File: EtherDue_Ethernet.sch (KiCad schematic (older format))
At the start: 32 parts, among them IC601 W5100, Q601 2N7002, U603 APX811-44UG-7, U604 HY931147C, X601 TXC 7A 25MHz 18pF

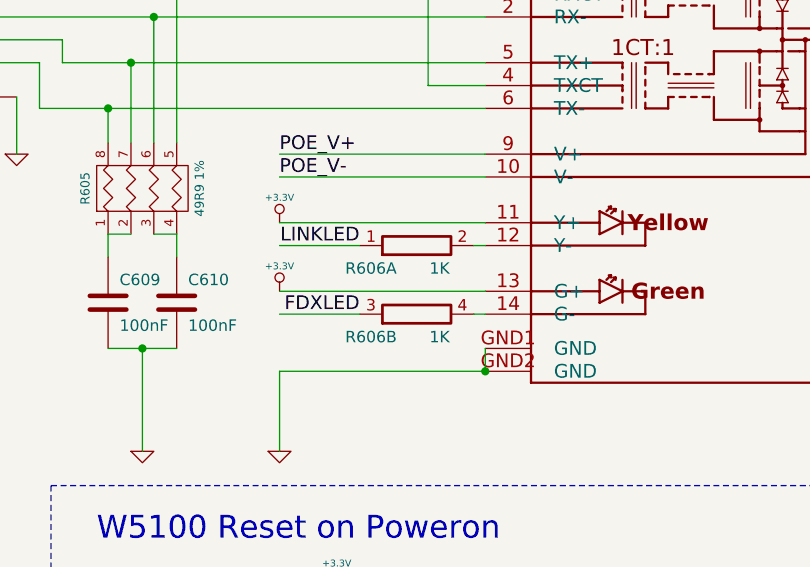
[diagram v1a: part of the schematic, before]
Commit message: Pre-autorouter hand routed traces
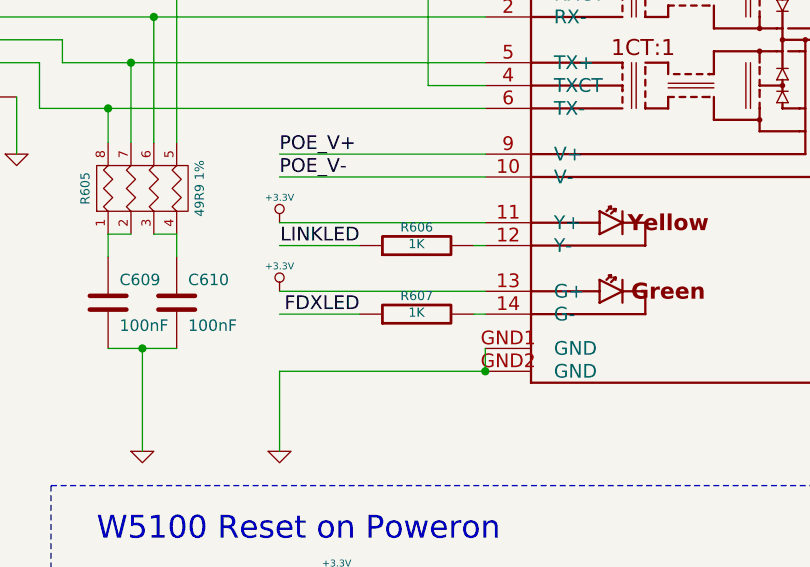
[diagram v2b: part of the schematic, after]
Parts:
- removed R606: 1K, symbol RES_PACK4_IND
- added R606, R607: 1K, ~, symbol R
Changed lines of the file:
@@
-EESchema Schematic File Version 2  date Thu 06 Jun 2013 17:31:40 EST
+EESchema Schematic File Version 2  date Wed 19 Jun 2013 10:44:48 EST
 LIBS:freetronics_kicad_sch_lib
 LIBS:power
@@
 Sheet 6 6
 Title ""
-Date "6 jun 2013"
+Date "19 jun 2013"
 Rev ""
 Comp ""
@@
 LINKLED
 $Comp
-L RES_PACK4_IND R606
-U 1 1 51663326
-P 8200 4300
-F 0 "R606" H 8000 4200 50  0000 C CNN
-F 1 "1K" H 8300 4200 50  0000 C CNN
-F 2 "" H 8200 4300 60  0001 C CNN
-F 3 "" H 8200 4300 60  0001 C CNN
-	1    8200 4300
-	1    0    0    -1
-$EndComp
-$Comp
-L RES_PACK4_IND R606
-U 2 1 51663316
-P 8200 4600
-F 0 "R606" H 8000 4500 50  0000 C CNN
-F 1 "1K" H 8300 4500 50  0000 C CNN
-F 2 "" H 8200 4600 60  0001 C CNN
-F 3 "" H 8200 4600 60  0001 C CNN
-	2    8200 4600
-	1    0    0    -1
-$EndComp
-$Comp
 L +3.3V #PWR091
 U 1 1 51663302
@@
 	1    0    0    -1
 $EndComp
+$Comp
+L R R606
+U 1 1 51C10B1D
+P 8200 4300
+F 0 "R606" V 8280 4300 40  0000 C CNN
+F 1 "1K" V 8207 4301 40  0000 C CNN
+F 2 "~" V 8130 4300 30  0000 C CNN
+F 3 "~" H 8200 4300 30  0000 C CNN
+	1    8200 4300
+	0    -1   -1   0
+$EndComp
+$Comp
+L R R607
+U 1 1 51C10B2F
+P 8200 4600
+F 0 "R607" V 8280 4600 40  0000 C CNN
+F 1 "1K" V 8207 4601 40  0000 C CNN
+F 2 "~" V 8130 4600 30  0000 C CNN
+F 3 "~" H 8200 4600 30  0000 C CNN
+	1    8200 4600
+	0    -1   -1   0
+$EndComp
 $EndSCHEMATC

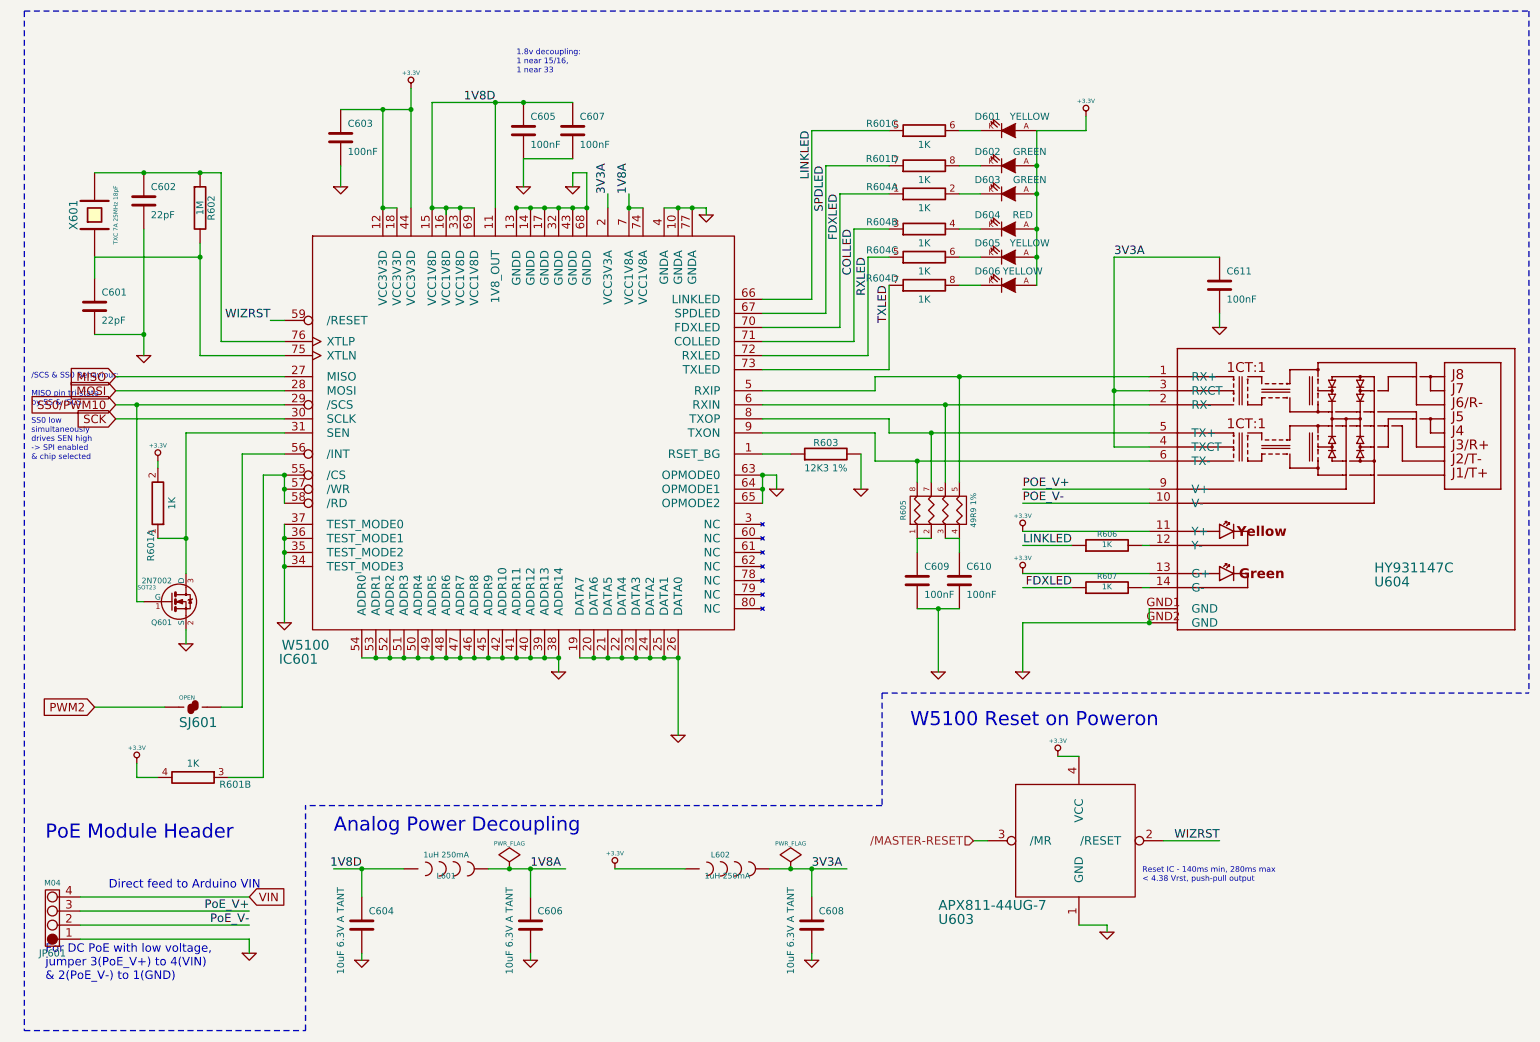
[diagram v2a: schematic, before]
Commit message: Add MicroSD card slot, ready for autorouter
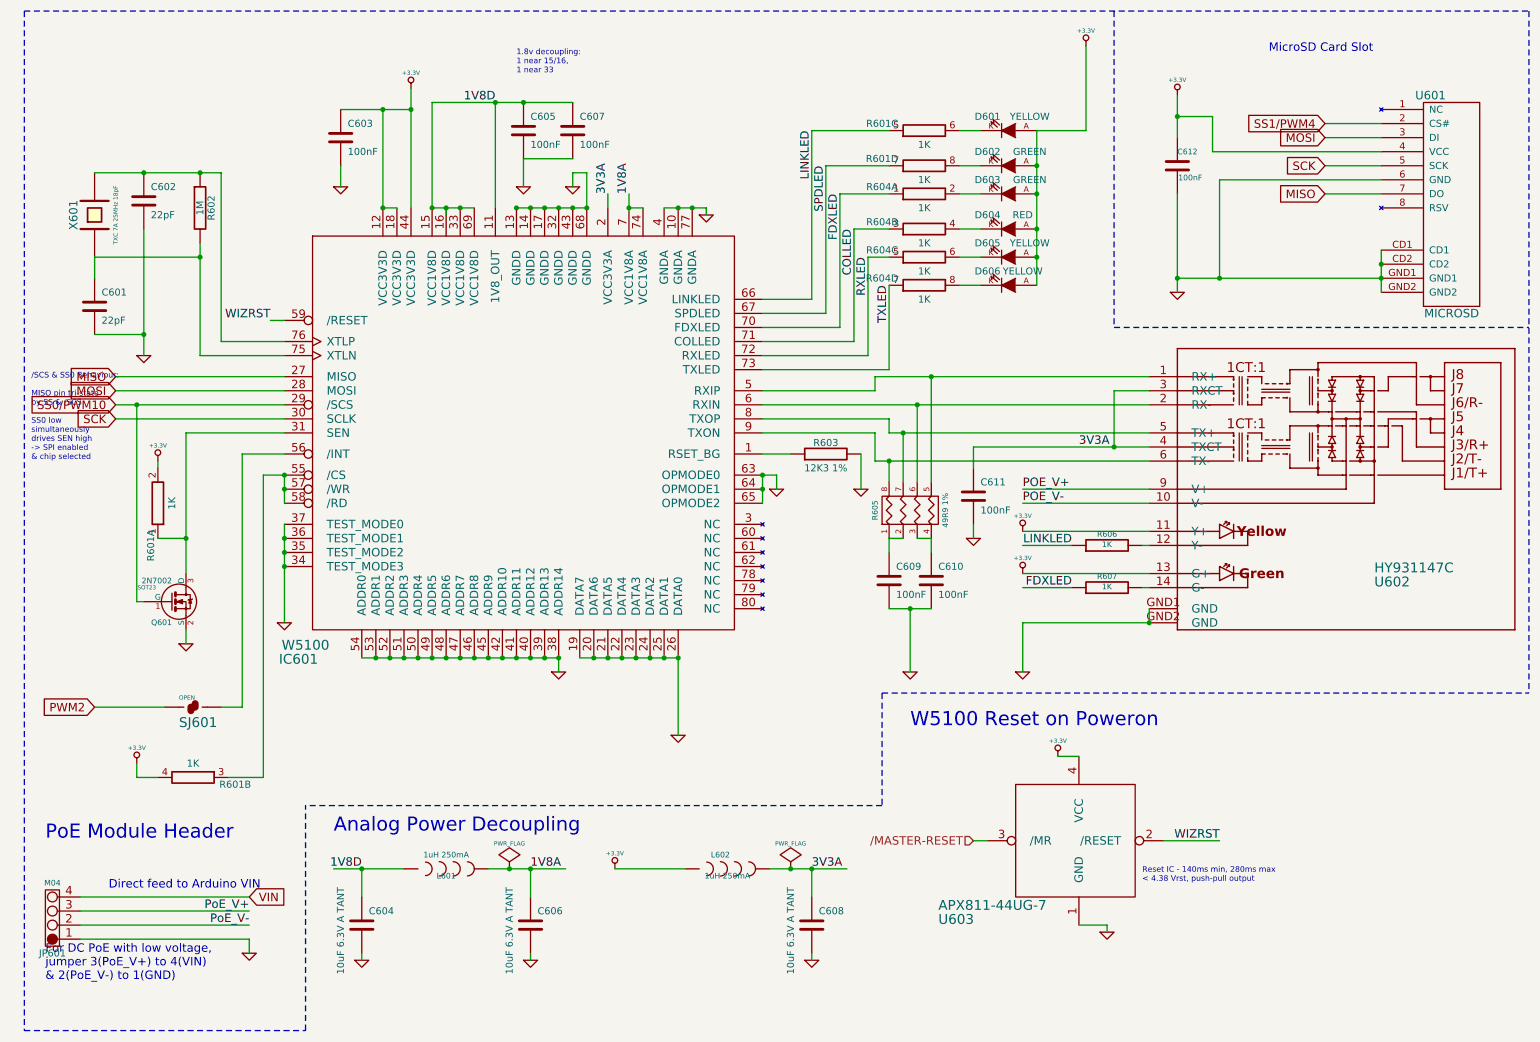
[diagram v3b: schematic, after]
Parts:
- added C612: 100nF, ~, symbol C
- added U601: MICROSD, ~, symbol MICROSD
- renumbered U604 to U602
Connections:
- net labels added: SS1/PWM4
- wire segments 144 -> 157
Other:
- note added: "MicroSD Card Slot"
- moved on the sheet: C609, C610, C611, R605

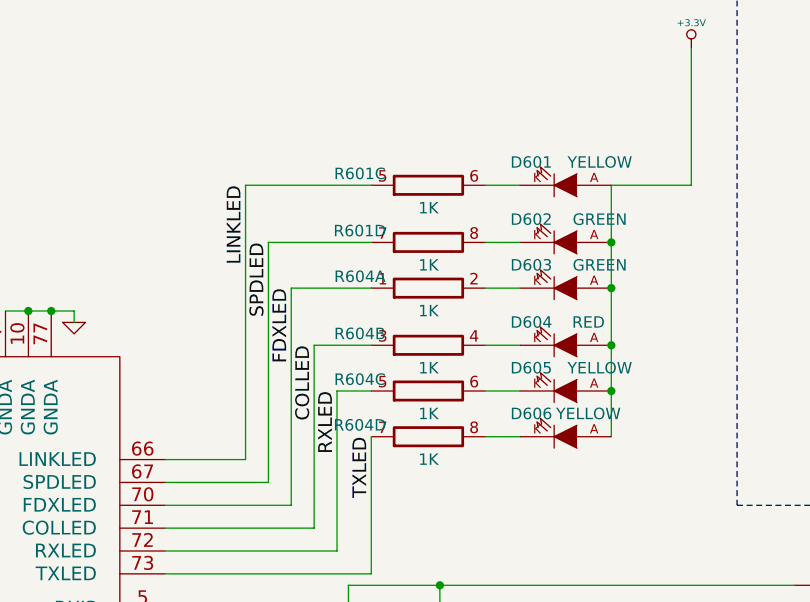
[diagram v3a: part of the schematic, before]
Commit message: Rearrange USB D+/D- traces for better clearances
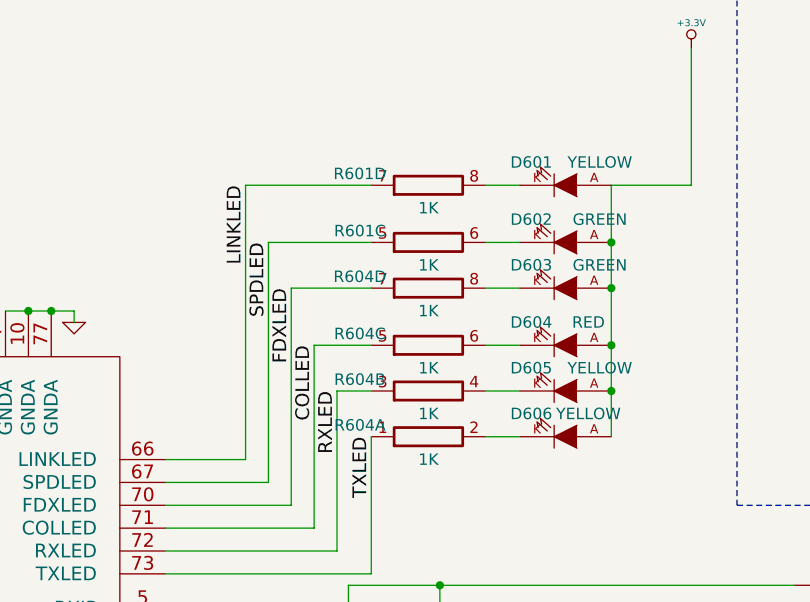
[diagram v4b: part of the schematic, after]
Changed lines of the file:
@@
-EESchema Schematic File Version 2  date Thu 27 Jun 2013 12:17:14 EST
+EESchema Schematic File Version 2  date Fri 28 Jun 2013 16:34:50 EST
 LIBS:freetronics_kicad_sch_lib
 LIBS:power
@@
 Connection ~ 3950 6600
 $Comp
-L PWR_FLAG #FLG602
+L PWR_FLAG #FLG079
 U 1 1 51663F3F
 P 5950 6600
-F 0 "#FLG602" H 5950 6695 30  0001 C CNN
+F 0 "#FLG079" H 5950 6695 30  0001 C CNN
 F 1 "PWR_FLAG" H 5950 6780 30  0000 C CNN
 F 2 "" H 5950 6600 60  0001 C CNN
@@
 $EndComp
 $Comp
-L PWR_FLAG #FLG601
+L PWR_FLAG #FLG080
 U 1 1 51663F3A
 P 3950 6600
-F 0 "#FLG601" H 3950 6695 30  0001 C CNN
+F 0 "#FLG080" H 3950 6695 30  0001 C CNN
 F 1 "PWR_FLAG" H 3950 6780 30  0000 C CNN
 F 2 "" H 3950 6600 60  0001 C CNN
@@
 $EndComp
 $Comp
-L GND #PWR627
+L GND #PWR081
 U 1 1 51663F24
 P 8200 7050
-F 0 "#PWR627" H 8200 7050 30  0001 C CNN
+F 0 "#PWR081" H 8200 7050 30  0001 C CNN
 F 1 "GND" H 8200 6980 30  0001 C CNN
 F 2 "" H 8200 7050 60  0001 C CNN
@@
 WIZRST
 $Comp
-L +3.3V #PWR625
+L +3.3V #PWR082
 U 1 1 51663BD9
 P 7850 5800
-F 0 "#PWR625" H 7850 5760 30  0001 C CNN
+F 0 "#PWR082" H 7850 5760 30  0001 C CNN
 F 1 "+3.3V" H 7850 5910 30  0000 C CNN
 F 2 "" H 7850 5800 60  0001 C CNN
@@
 W5100 Reset on Poweron
 $Comp
-L +3.3V #PWR614
+L +3.3V #PWR083
 U 1 1 51663ACF
 P 4700 6600
-F 0 "#PWR614" H 4700 6560 30  0001 C CNN
+F 0 "#PWR083" H 4700 6560 30  0001 C CNN
 F 1 "+3.3V" H 4700 6710 30  0000 C CNN
 F 2 "" H 4700 6600 60  0001 C CNN
@@
 $EndComp
 $Comp
-L GND #PWR618
+L GND #PWR084
 U 1 1 51663ACA
 P 6100 7250
-F 0 "#PWR618" H 6100 7250 30  0001 C CNN
+F 0 "#PWR084" H 6100 7250 30  0001 C CNN
 F 1 "GND" H 6100 7180 30  0001 C CNN
 F 2 "" H 6100 7250 60  0001 C CNN
@@
 1V8D
 $Comp
-L GND #PWR611
+L GND #PWR085
 U 1 1 51663AAD
 P 4100 7250
-F 0 "#PWR611" H 4100 7250 30  0001 C CNN
+F 0 "#PWR085" H 4100 7250 30  0001 C CNN
 F 1 "GND" H 4100 7180 30  0001 C CNN
 F 2 "" H 4100 7250 60  0001 C CNN
@@
 $EndComp
 $Comp
-L GND #PWR608
+L GND #PWR086
 U 1 1 51663A9A
 P 2900 7250
-F 0 "#PWR608" H 2900 7250 30  0001 C CNN
+F 0 "#PWR086" H 2900 7250 30  0001 C CNN
 F 1 "GND" H 2900 7180 30  0001 C CNN
 F 2 "" H 2900 7250 60  0001 C CNN
@@
 Analog Power Decoupling\n
 $Comp
-L GND #PWR620
+L GND #PWR087
 U 1 1 516639AE
 P 6800 5200
-F 0 "#PWR620" H 6800 5200 30  0001 C CNN
+F 0 "#PWR087" H 6800 5200 30  0001 C CNN
 F 1 "GND" H 6800 5130 30  0001 C CNN
 F 2 "" H 6800 5200 60  0001 C CNN
@@
 $EndComp
 $Comp
-L +3.3V #PWR622
+L +3.3V #PWR088
 U 1 1 51663851
 P 7600 4200
-F 0 "#PWR622" H 7600 4160 30  0001 C CNN
+F 0 "#PWR088" H 7600 4160 30  0001 C CNN
 F 1 "+3.3V" H 7600 4310 30  0000 C CNN
 F 2 "" H 7600 4200 60  0001 C CNN
@@
 For DC PoE with low voltage,\njumper 3(PoE_V+) to 4(VIN)\n& 2(PoE_V-) to 1(GND)
 $Comp
-L GND #PWR605
+L GND #PWR089
 U 1 1 516634EC
 P 2100 7200
-F 0 "#PWR605" H 2100 7200 30  0001 C CNN
+F 0 "#PWR089" H 2100 7200 30  0001 C CNN
 F 1 "GND" H 2100 7130 30  0001 C CNN
 F 2 "" H 2100 7200 60  0001 C CNN
@@
 PoE Module Header
 $Comp
-L GND #PWR624
+L GND #PWR090
 U 1 1 51663438
 P 7600 5200
-F 0 "#PWR624" H 7600 5200 30  0001 C CNN
+F 0 "#PWR090" H 7600 5200 30  0001 C CNN
 F 1 "GND" H 7600 5130 30  0001 C CNN
 F 2 "" H 7600 5200 60  0001 C CNN
@@
 LINKLED
 $Comp
-L +3.3V #PWR623
+L +3.3V #PWR091
 U 1 1 51663302
 P 7600 4500
-F 0 "#PWR623" H 7600 4460 30  0001 C CNN
+F 0 "#PWR091" H 7600 4460 30  0001 C CNN
 F 1 "+3.3V" H 7600 4610 30  0000 C CNN
 F 2 "" H 7600 4500 60  0001 C CNN
@@
 $EndComp
 $Comp
-L GND #PWR621
+L GND #PWR092
 U 1 1 516632C9
 P 7250 4250
-F 0 "#PWR621" H 7250 4250 30  0001 C CNN
+F 0 "#PWR092" H 7250 4250 30  0001 C CNN
 F 1 "GND" H 7250 4180 30  0001 C CNN
 F 2 "" H 7250 4250 60  0001 C CNN
@@
 3V3A
 $Comp
-L GND #PWR607
+L GND #PWR093
 U 1 1 516630F1
 P 2750 1750
-F 0 "#PWR607" H 2750 1750 30  0001 C CNN
+F 0 "#PWR093" H 2750 1750 30  0001 C CNN
 F 1 "GND" H 2750 1680 30  0001 C CNN
 F 2 "" H 2750 1750 60  0001 C CNN
@@
 $EndComp
 $Comp
-L +3.3V #PWR609
+L +3.3V #PWR094
 U 1 1 516630E9
 P 3250 1050
-F 0 "#PWR609" H 3250 1010 30  0001 C CNN
+F 0 "#PWR094" H 3250 1010 30  0001 C CNN
 F 1 "+3.3V" H 3250 1160 30  0000 C CNN
 F 2 "" H 3250 1050 60  0001 C CNN
@@
 1.8v decoupling:\n1 near 15/16,\n1 near 33
 $Comp
-L GND #PWR610
+L GND #PWR095
 U 1 1 51662F42
 P 4050 1750
-F 0 "#PWR610" H 4050 1750 30  0001 C CNN
+F 0 "#PWR095" H 4050 1750 30  0001 C CNN
 F 1 "GND" H 4050 1680 30  0001 C CNN
 F 2 "" H 4050 1750 60  0001 C CNN
@@
 LINKLED
 $Comp
-L +3.3V #PWR626
+L +3.3V #PWR096
 U 1 1 51662070
 P 8050 750
-F 0 "#PWR626" H 8050 710 30  0001 C CNN
+F 0 "#PWR096" H 8050 710 30  0001 C CNN
 F 1 "+3.3V" H 8050 860 30  0000 C CNN
 F 2 "" H 8050 750 60  0001 C CNN
@@
 $Comp
 L RES_PACK4_IND R604
-U 4 1 51661F97
+U 1 1 51661F97
 P 6900 2450
 F 0 "R604" H 6600 2500 50  0000 C CNN
@@
 F 2 "" H 6900 2450 60  0001 C CNN
 F 3 "" H 6900 2450 60  0001 C CNN
-	4    6900 2450
+	1    6900 2450
 	1    0    0    -1
 $EndComp
 $Comp
 L RES_PACK4_IND R604
-U 3 1 51661F96
+U 2 1 51661F96
 P 6900 2250
 F 0 "R604" H 6600 2300 50  0000 C CNN
@@
 F 2 "" H 6900 2250 60  0001 C CNN
 F 3 "" H 6900 2250 60  0001 C CNN
-	3    6900 2250
+	2    6900 2250
 	1    0    0    -1
 $EndComp
 $Comp
 L RES_PACK4_IND R604
-U 1 1 51661F8E
+U 4 1 51661F8E
 P 6900 1800
 F 0 "R604" H 6600 1850 50  0000 C CNN
@@
 F 2 "" H 6900 1800 60  0001 C CNN
 F 3 "" H 6900 1800 60  0001 C CNN
-	1    6900 1800
+	4    6900 1800
 	1    0    0    -1
 $EndComp
 $Comp
 L RES_PACK4_IND R604
-U 2 1 51661F8D
+U 3 1 51661F8D
 P 6900 2050
 F 0 "R604" H 6600 2100 50  0000 C CNN
@@
 F 2 "" H 6900 2050 60  0001 C CNN
 F 3 "" H 6900 2050 60  0001 C CNN
-	2    6900 2050
+	3    6900 2050
 	1    0    0    -1
 $EndComp
 $Comp
 L RES_PACK4_IND R601
-U 4 1 51661F61
+U 3 1 51661F61
 P 6900 1600
 F 0 "R601" H 6600 1650 50  0000 C CNN
@@
 F 2 "" H 6900 1600 60  0001 C CNN
 F 3 "" H 6900 1600 60  0001 C CNN
-	4    6900 1600
+	3    6900 1600
 	1    0    0    -1
 $EndComp
 $Comp
 L RES_PACK4_IND R601
-U 3 1 51661F57
+U 4 1 51661F57
 P 6900 1350
 F 0 "R601" H 6600 1400 50  0000 C CNN
@@
 F 2 "" H 6900 1350 60  0001 C CNN
 F 3 "" H 6900 1350 60  0001 C CNN
-	3    6900 1350
+	4    6900 1350
 	1    0    0    -1
 $EndComp
@@
 PWM2
 $Comp
-L GND #PWR602
+L GND #PWR097
 U 1 1 51661CDB
 P 1350 2950
-F 0 "#PWR602" H 1350 2950 30  0001 C CNN
+F 0 "#PWR097" H 1350 2950 30  0001 C CNN
 F 1 "GND" H 1350 2880 30  0001 C CNN
 F 2 "" H 1350 2950 60  0001 C CNN
@@
 WIZRST
 $Comp
-L GND #PWR613
+L GND #PWR098
 U 1 1 51661C24
 P 4400 1750
-F 0 "#PWR613" H 4400 1750 30  0001 C CNN
+F 0 "#PWR098" H 4400 1750 30  0001 C CNN
 F 1 "GND" H 4400 1680 30  0001 C CNN
 F 2 "" H 4400 1750 60  0001 C CNN
@@
 $EndComp
 $Comp
-L GND #PWR616
+L GND #PWR099
 U 1 1 51661C10
 P 5350 1950
-F 0 "#PWR616" H 5350 1950 30  0001 C CNN
+F 0 "#PWR099" H 5350 1950 30  0001 C CNN
 F 1 "GND" H 5350 1880 30  0001 C CNN
 F 2 "" H 5350 1950 60  0001 C CNN
@@
 $EndComp
 $Comp
-L GND #PWR619
+L GND #PWR0100
 U 1 1 51661BE8
 P 6450 3900
-F 0 "#PWR619" H 6450 3900 30  0001 C CNN
+F 0 "#PWR0100" H 6450 3900 30  0001 C CNN
 F 1 "GND" H 6450 3830 30  0001 C CNN
 F 2 "" H 6450 3900 60  0001 C CNN
@@
 $EndComp
 $Comp
-L GND #PWR617
+L GND #PWR0101
 U 1 1 51661BC5
 P 5850 3900
-F 0 "#PWR617" H 5850 3900 30  0001 C CNN
+F 0 "#PWR0101" H 5850 3900 30  0001 C CNN
 F 1 "GND" H 5850 3830 30  0001 C CNN
 F 2 "" H 5850 3900 60  0001 C CNN
@@
 $EndComp
 $Comp
-L GND #PWR612
+L GND #PWR0102
 U 1 1 51661B99
 P 4300 5200
-F 0 "#PWR612" H 4300 5200 30  0001 C CNN
+F 0 "#PWR0102" H 4300 5200 30  0001 C CNN
 F 1 "GND" H 4300 5130 30  0001 C CNN
 F 2 "" H 4300 5200 60  0001 C CNN
@@
 $EndComp
 $Comp
-L GND #PWR615
+L GND #PWR0103
 U 1 1 51661B97
 P 5150 5650
-F 0 "#PWR615" H 5150 5650 30  0001 C CNN
+F 0 "#PWR0103" H 5150 5650 30  0001 C CNN
 F 1 "GND" H 5150 5580 30  0001 C CNN
 F 2 "" H 5150 5650 60  0001 C CNN
@@
 $EndComp
 $Comp
-L GND #PWR606
+L GND #PWR0104
 U 1 1 51661B24
 P 2350 4850
-F 0 "#PWR606" H 2350 4850 30  0001 C CNN
+F 0 "#PWR0104" H 2350 4850 30  0001 C CNN
 F 1 "GND" H 2350 4780 30  0001 C CNN
 F 2 "" H 2350 4850 60  0001 C CNN
@@
 $EndComp
 $Comp
-L +3.3V #PWR601
+L +3.3V #PWR0105
 U 1 1 51661B00
 P 1300 5850
-F 0 "#PWR601" H 1300 5810 30  0001 C CNN
+F 0 "#PWR0105" H 1300 5810 30  0001 C CNN
 F 1 "+3.3V" H 1300 5960 30  0000 C CNN
 F 2 "" H 1300 5850 60  0001 C CNN
@@
 $EndComp
 $Comp
-L +3.3V #PWR603
+L +3.3V #PWR0106
 U 1 1 5166191F
 P 1450 3700
-F 0 "#PWR603" H 1450 3660 30  0001 C CNN
+F 0 "#PWR0106" H 1450 3660 30  0001 C CNN
 F 1 "+3.3V" H 1450 3810 30  0000 C CNN
 F 2 "" H 1450 3700 60  0001 C CNN
@@
 $EndComp
 $Comp
-L GND #PWR604
+L GND #PWR0107
 U 1 1 516618BF
 P 1650 5000
-F 0 "#PWR604" H 1650 5000 30  0001 C CNN
+F 0 "#PWR0107" H 1650 5000 30  0001 C CNN
 F 1 "GND" H 1650 4930 30  0001 C CNN
 F 2 "" H 1650 5000 60  0001 C CNN
@@
 $EndComp
 $Comp
-L +3.3V #PWR628
+L +3.3V #PWR0108
 U 1 1 51CBA5E1
 P 8700 1100
-F 0 "#PWR628" H 8700 1060 30  0001 C CNN
+F 0 "#PWR0108" H 8700 1060 30  0001 C CNN
 F 1 "+3.3V" H 8700 1210 30  0000 C CNN
 F 2 "" H 8700 1100 60  0000 C CNN
@@
 Connection ~ 8700 2400
 $Comp
-L GND #PWR629
+L GND #PWR0109
 U 1 1 51CBA9E0
 P 8700 2500
-F 0 "#PWR629" H 8700 2500 30  0001 C CNN
+F 0 "#PWR0109" H 8700 2500 30  0001 C CNN
 F 1 "GND" H 8700 2430 30  0001 C CNN
 F 2 "" H 8700 2500 60  0000 C CNN
